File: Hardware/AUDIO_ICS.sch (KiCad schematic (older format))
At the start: 41 parts, among them U10 PCM1863, U9 PCM9211, X1 24.576 MHz

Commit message: Completed placement of level shifters
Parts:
- C36: footprint Capacitors_SMD:c_elec_4x4.5 -> Capacitors_SMD:C_1206
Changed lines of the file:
@@
 F 0 "C36" H 1750 10700 40  0000 L CNN
 F 1 "10uF" H 1756 10515 40  0000 L CNN
-F 2 "Capacitors_SMD:c_elec_4x4.5" H 1788 10450 30  0001 C CNN
+F 2 "Capacitors_SMD:C_1206" H 1788 10450 30  0001 C CNN
 F 3 "" H 1750 10600 60  0000 C CNN
 	1    1750 10600
@@
 	6000 4950 6000 4400
 Wire Wire Line
-	5450 4950 5700 4950
-Wire Wire Line
-	5700 4950 6000 4950
+	5450 4950 6000 4950
 Wire Wire Line
 	2850 4500 2850 5100
@@
 	4800 2000 6000 2000
 Wire Wire Line
-	6100 7450 6100 7550
-Wire Wire Line
-	6100 7550 6100 9700
+	6100 7450 6100 9700
 Wire Wire Line
 	6300 2200 4800 2200
@@
 Connection ~ 5400 1500
 Wire Wire Line
-	5100 1500 5400 1500
-Wire Wire Line
-	5400 1500 5550 1500
-Wire Wire Line
-	5550 1500 5700 1500
-Wire Wire Line
-	5700 1500 6000 1500
+	5100 1500 6000 1500
 Wire Wire Line
 	5100 1500 5100 1350
@@
 	2800 10900 2800 11000
 Wire Wire Line
-	2650 10900 2800 10900
-Wire Wire Line
-	2800 10900 2950 10900
+	2650 10900 2950 10900
 Wire Wire Line
 	2650 10750 2650 10900
@@
 	2800 10300 2800 10250
 Wire Wire Line
-	2650 10300 2800 10300
-Wire Wire Line
-	2800 10300 2950 10300
+	2650 10300 2950 10300
 Wire Wire Line
 	2650 10300 2650 10450
@@
 	1750 10750 1750 10900
 Wire Wire Line
-	1750 10900 1750 10900
-Wire Wire Line
-	1750 10900 1900 10900
-Wire Wire Line
-	1900 10900 2050 10900
-Wire Wire Line
-	2050 10900 2050 10900
+	1750 10900 2050 10900
 Wire Wire Line
 	1900 10900 1900 11000
@@
 	1900 10300 1900 10250
 Wire Wire Line
-	1750 10300 1750 10300
-Wire Wire Line
-	1750 10300 1900 10300
-Wire Wire Line
-	1900 10300 2050 10300
-Wire Wire Line
-	2050 10300 2050 10300
+	1750 10300 2050 10300
 Wire Wire Line
 	1750 10300 1750 10450
@@
 Connection ~ 2950 2600
 Wire Wire Line
-	2950 2500 2950 2600
-Wire Wire Line
-	2950 2600 2950 2900
+	2950 2500 2950 2900
 Wire Wire Line
 	2950 2600 3100 2600
@@
 	2950 1500 3100 1500
 Wire Wire Line
-	2950 1300 2950 1500
-Wire Wire Line
-	2950 1500 2950 1600
-Wire Wire Line
-	2950 1600 2950 1700
+	2950 1300 2950 1700
 Wire Wire Line
 	2950 2000 3100 2000
 Wire Wire Line
-	2950 1800 2950 2000
-Wire Wire Line
-	2950 2000 2950 2250
+	2950 1800 2950 2250
 Wire Wire Line
 	3100 2100 2300 2100
@@
 	2100 4850 2250 4850
 Wire Wire Line
-	2100 4100 2100 4500
-Wire Wire Line
-	2100 4500 2100 4850
-Wire Wire Line
-	2100 4850 2100 5100
+	2100 4100 2100 5100
 Wire Wire Line
 	2100 4100 2250 4100
@@
 	5700 3800 5700 4550
 Wire Wire Line
-	4800 3800 5450 3800
-Wire Wire Line
-	5450 3800 5700 3800
+	4800 3800 5700 3800
 Wire Wire Line
 	5450 3800 5450 4000
@@
 	5300 4200 4800 4200
 Wire Wire Line
-	5300 4000 5300 4100
-Wire Wire Line
-	5300 4100 5300 4200
-Wire Wire Line
-	5300 4200 5300 4300
-Wire Wire Line
-	5300 4300 5300 5100
+	5300 4000 5300 5100
 Wire Wire Line
 	5300 4300 4800 4300
@@
 	4900 4400 4900 4550
 Wire Wire Line
-	4800 4400 4900 4400
-Wire Wire Line
-	4900 4400 5150 4400
-Wire Wire Line
-	1650 7000 1950 7000
-Wire Wire Line
-	1950 7000 3350 7000
-Wire Wire Line
-	1650 6800 2100 6800
-Wire Wire Line
-	2100 6800 3350 6800
-Wire Wire Line
-	1650 6550 2250 6550
-Wire Wire Line
-	2250 6550 3350 6550
-Wire Wire Line
-	1650 6350 2400 6350
-Wire Wire Line
-	2400 6350 3350 6350
+	4800 4400 5150 4400
+Wire Wire Line
+	1650 7000 3350 7000
+Wire Wire Line
+	1650 6800 3350 6800
+Wire Wire Line
+	1650 6550 3350 6550
+Wire Wire Line
+	1650 6350 3350 6350
 Wire Wire Line
 	2400 7450 2400 7600
@@
 Connection ~ 2700 4100
 Wire Wire Line
-	2550 4100 2700 4100
-Wire Wire Line
-	2700 4100 3100 4100
+	2550 4100 3100 4100
 Wire Wire Line
 	2700 4100 2700 4300
 Wire Wire Line
-	2550 4850 2700 4850
-Wire Wire Line
-	2700 4850 2950 4850
+	2550 4850 2950 4850
 Wire Wire Line
 	2700 4700 2700 4850
 Wire Wire Line
-	4150 6150 4150 6800
-Wire Wire Line
-	4150 6800 4150 6900
+	4150 6150 4150 6900
 Wire Wire Line
 	4150 6800 4250 6800
@@
 	4250 8750 4250 9050
 Wire Wire Line
-	5950 8550 5950 8650
-Wire Wire Line
-	5950 8650 5950 8750
-Wire Wire Line
-	5950 8750 5950 9700
+	5950 8550 5950 9700
 Wire Wire Line
 	5950 8750 5850 8750
@@
 	3900 7200 4250 7200
 Wire Wire Line
-	1650 7850 2400 7850
-Wire Wire Line
-	2400 7850 3200 7850
-Wire Wire Line
-	3200 7850 3350 7850
-Wire Wire Line
-	1650 8050 2250 8050
-Wire Wire Line
-	2250 8050 3050 8050
-Wire Wire Line
-	3050 8050 3350 8050
-Wire Wire Line
-	1650 8300 2100 8300
-Wire Wire Line
-	2100 8300 2900 8300
-Wire Wire Line
-	2900 8300 3350 8300
-Wire Wire Line
-	1650 8500 1950 8500
-Wire Wire Line
-	1950 8500 2750 8500
-Wire Wire Line
-	2750 8500 3350 8500
+	1650 7850 3350 7850
+Wire Wire Line
+	1650 8050 3350 8050
+Wire Wire Line
+	1650 8300 3350 8300
+Wire Wire Line
+	1650 8500 3350 8500
 Wire Wire Line
 	2400 9350 2400 9700
@@
 	3950 9350 3950 9700
 Wire Wire Line
-	3950 8200 3950 8900
-Wire Wire Line
-	3950 8900 3950 9050
+	3950 8200 3950 9050
 Wire Wire Line
 	3950 8200 4250 8200
@@
 	3200 9550 3200 9350
 Wire Wire Line
-	2750 9550 2900 9550
-Wire Wire Line
-	2900 9550 3050 9550
-Wire Wire Line
-	3050 9550 3200 9550
-Wire Wire Line
-	3200 9550 3550 9550
+	2750 9550 3550 9550
 Wire Wire Line
 	3550 9550 3550 8900
@@
 Connection ~ 5700 1500
 Wire Wire Line
-	5100 900  5400 900
-Wire Wire Line
-	5400 900  5550 900
-Wire Wire Line
-	5550 900  5700 900
-Wire Wire Line
-	5700 900  6000 900
+	5100 900  6000 900
 Connection ~ 5550 900
 Wire Wire Line

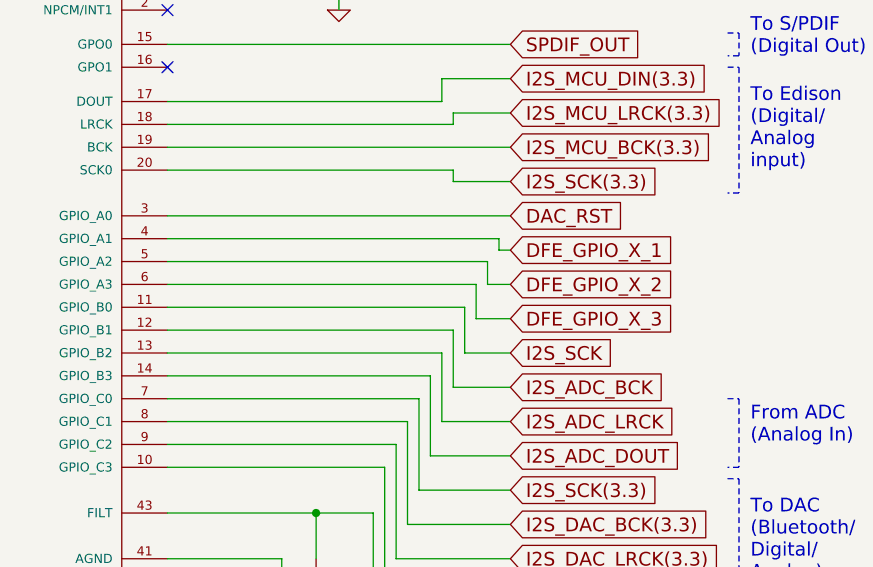
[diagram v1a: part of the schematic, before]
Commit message: Digital Half completed placement
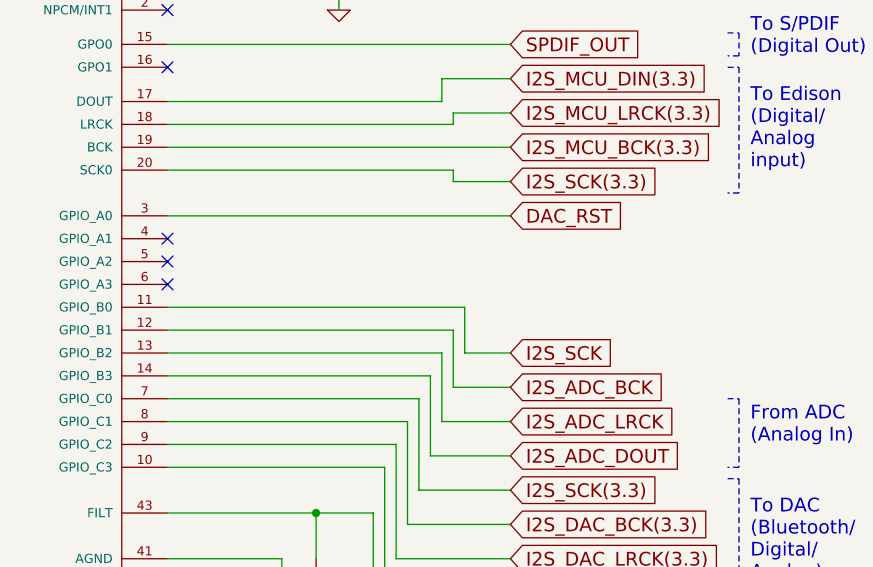
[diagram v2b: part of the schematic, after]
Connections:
- net DFE_GPIO_X_1: no longer names the net of U9.4 (GPIO_A1)
- net DFE_GPIO_X_2: no longer names the net of U9.5 (GPIO_A2)
- net DFE_GPIO_X_3: no longer names the net of U9.6 (GPIO_A3)
- no-connect marks 12 -> 15
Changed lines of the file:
@@
 ADC unused\nAnalog VCC\nGrounded
 $Comp
-L +3.3VSB #PWR039
+L +3.3VSB #PWR036
 U 1 1 57F2FC3A
 P 2950 1300
-F 0 "#PWR039" H 2950 1260 30  0001 C CNN
+F 0 "#PWR036" H 2950 1260 30  0001 C CNN
 F 1 "+3.3VSB" H 2950 1400 30  0000 C CNN
 F 2 "" H 2950 1300 60  0000 C CNN
@@
 Pulled LOW for\nI2C mode
 $Comp
-L GND-RESCUE-museV2-RESCUE-museV2 #PWR040
+L GND-RESCUE-museV2-RESCUE-museV2 #PWR037
 U 1 1 57F2FC41
 P 2950 2250
-F 0 "#PWR040" H 2950 2250 30  0001 C CNN
+F 0 "#PWR037" H 2950 2250 30  0001 C CNN
 F 1 "GND" H 2950 2180 30  0001 C CNN
 F 2 "" H 2950 2250 60  0000 C CNN
@@
 $EndComp
 $Comp
-L GND-RESCUE-museV2-RESCUE-museV2 #PWR041
+L GND-RESCUE-museV2-RESCUE-museV2 #PWR038
 U 1 1 57F2FC5D
 P 2100 5100
-F 0 "#PWR041" H 2100 5100 30  0001 C CNN
+F 0 "#PWR038" H 2100 5100 30  0001 C CNN
 F 1 "GND" H 2100 5030 30  0001 C CNN
 F 2 "" H 2100 5100 60  0000 C CNN
@@
 $EndComp
 $Comp
-L GND-RESCUE-museV2-RESCUE-museV2 #PWR042
+L GND-RESCUE-museV2-RESCUE-museV2 #PWR039
 U 1 1 57F2FC84
 P 5300 5100
-F 0 "#PWR042" H 5300 5100 30  0001 C CNN
+F 0 "#PWR039" H 5300 5100 30  0001 C CNN
 F 1 "GND" H 5300 5030 30  0001 C CNN
 F 2 "" H 5300 5100 60  0000 C CNN
@@
 $EndComp
 $Comp
-L GND-RESCUE-museV2-RESCUE-museV2 #PWR043
+L GND-RESCUE-museV2-RESCUE-museV2 #PWR040
 U 1 1 57F2FC8A
 P 5150 5100
-F 0 "#PWR043" H 5150 5100 30  0001 C CNN
+F 0 "#PWR040" H 5150 5100 30  0001 C CNN
 F 1 "GND" H 5150 5030 30  0001 C CNN
 F 2 "" H 5150 5100 60  0000 C CNN
@@
 $EndComp
 $Comp
-L GND-RESCUE-museV2-RESCUE-museV2 #PWR044
+L GND-RESCUE-museV2-RESCUE-museV2 #PWR041
 U 1 1 57F2FC90
 P 4900 5100
-F 0 "#PWR044" H 4900 5100 30  0001 C CNN
+F 0 "#PWR041" H 4900 5100 30  0001 C CNN
 F 1 "GND" H 4900 5030 30  0001 C CNN
 F 2 "" H 4900 5100 60  0000 C CNN
@@
 $EndComp
 $Comp
-L GND-RESCUE-museV2-RESCUE-museV2 #PWR045
+L GND-RESCUE-museV2-RESCUE-museV2 #PWR042
 U 1 1 57F2FCAF
 P 2400 7600
-F 0 "#PWR045" H 2400 7600 30  0001 C CNN
+F 0 "#PWR042" H 2400 7600 30  0001 C CNN
 F 1 "GND" H 2400 7530 30  0001 C CNN
 F 2 "" H 2400 7600 60  0000 C CNN
@@
 $EndComp
 $Comp
-L GND-RESCUE-museV2-RESCUE-museV2 #PWR046
+L GND-RESCUE-museV2-RESCUE-museV2 #PWR043
 U 1 1 57F2FCB5
 P 2250 7600
-F 0 "#PWR046" H 2250 7600 30  0001 C CNN
+F 0 "#PWR043" H 2250 7600 30  0001 C CNN
 F 1 "GND" H 2250 7530 30  0001 C CNN
 F 2 "" H 2250 7600 60  0000 C CNN
@@
 $EndComp
 $Comp
-L GND-RESCUE-museV2-RESCUE-museV2 #PWR047
+L GND-RESCUE-museV2-RESCUE-museV2 #PWR044
 U 1 1 57F2FCBB
 P 2100 7600
-F 0 "#PWR047" H 2100 7600 30  0001 C CNN
+F 0 "#PWR044" H 2100 7600 30  0001 C CNN
 F 1 "GND" H 2100 7530 30  0001 C CNN
 F 2 "" H 2100 7600 60  0000 C CNN
@@
 $EndComp
 $Comp
-L GND-RESCUE-museV2-RESCUE-museV2 #PWR048
+L GND-RESCUE-museV2-RESCUE-museV2 #PWR045
 U 1 1 57F2FCC1
 P 1950 7600
-F 0 "#PWR048" H 1950 7600 30  0001 C CNN
+F 0 "#PWR045" H 1950 7600 30  0001 C CNN
 F 1 "GND" H 1950 7530 30  0001 C CNN
 F 2 "" H 1950 7600 60  0000 C CNN
@@
 $EndComp
 $Comp
-L +3.3VSB #PWR049
+L +3.3VSB #PWR046
 U 1 1 57F2FD06
 P 4150 6150
-F 0 "#PWR049" H 4150 6110 30  0001 C CNN
+F 0 "#PWR046" H 4150 6110 30  0001 C CNN
 F 1 "+3.3VSB" H 4150 6260 30  0000 C CNN
 F 2 "" H 4150 6150 60  0000 C CNN
@@
 $EndComp
 $Comp
-L +1.8VSB #PWR050
+L +1.8VSB #PWR047
 U 1 1 57F2FD0C
 P 3950 6150
-F 0 "#PWR050" H 3950 6290 20  0001 C CNN
+F 0 "#PWR047" H 3950 6290 20  0001 C CNN
 F 1 "+1.8VSB" H 3950 6260 30  0000 C CNN
 F 2 "" H 3950 6150 60  0000 C CNN
@@
 PCM1863 (ADC)
 $Comp
-L GND-RESCUE-museV2-RESCUE-museV2 #PWR051
+L GND-RESCUE-museV2-RESCUE-museV2 #PWR048
 U 1 1 57F2FD1E
 P 5950 9700
-F 0 "#PWR051" H 5950 9700 30  0001 C CNN
+F 0 "#PWR048" H 5950 9700 30  0001 C CNN
 F 1 "GND" H 5950 9630 30  0001 C CNN
 F 2 "" H 5950 9700 60  0000 C CNN
@@
 $EndComp
 $Comp
-L GND-RESCUE-museV2-RESCUE-museV2 #PWR052
+L GND-RESCUE-museV2-RESCUE-museV2 #PWR049
 U 1 1 57F2FD2B
 P 4250 9700
-F 0 "#PWR052" H 4250 9700 30  0001 C CNN
+F 0 "#PWR049" H 4250 9700 30  0001 C CNN
 F 1 "GND" H 4250 9630 30  0001 C CNN
 F 2 "" H 4250 9700 60  0000 C CNN
@@
 $EndComp
 $Comp
-L GND-RESCUE-museV2-RESCUE-museV2 #PWR053
+L GND-RESCUE-museV2-RESCUE-museV2 #PWR050
 U 1 1 57F2FD4E
 P 2400 9700
-F 0 "#PWR053" H 2400 9700 30  0001 C CNN
+F 0 "#PWR050" H 2400 9700 30  0001 C CNN
 F 1 "GND" H 2400 9630 30  0001 C CNN
 F 2 "" H 2400 9700 60  0000 C CNN
@@
 $EndComp
 $Comp
-L GND-RESCUE-museV2-RESCUE-museV2 #PWR054
+L GND-RESCUE-museV2-RESCUE-museV2 #PWR051
 U 1 1 57F2FD54
 P 2250 9700
-F 0 "#PWR054" H 2250 9700 30  0001 C CNN
+F 0 "#PWR051" H 2250 9700 30  0001 C CNN
 F 1 "GND" H 2250 9630 30  0001 C CNN
 F 2 "" H 2250 9700 60  0000 C CNN
@@
 $EndComp
 $Comp
-L GND-RESCUE-museV2-RESCUE-museV2 #PWR055
+L GND-RESCUE-museV2-RESCUE-museV2 #PWR052
 U 1 1 57F2FD5A
 P 2100 9700
-F 0 "#PWR055" H 2100 9700 30  0001 C CNN
+F 0 "#PWR052" H 2100 9700 30  0001 C CNN
 F 1 "GND" H 2100 9630 30  0001 C CNN
 F 2 "" H 2100 9700 60  0000 C CNN
@@
 $EndComp
 $Comp
-L GND-RESCUE-museV2-RESCUE-museV2 #PWR056
+L GND-RESCUE-museV2-RESCUE-museV2 #PWR053
 U 1 1 57F2FD60
 P 1950 9700
-F 0 "#PWR056" H 1950 9700 30  0001 C CNN
+F 0 "#PWR053" H 1950 9700 30  0001 C CNN
 F 1 "GND" H 1950 9630 30  0001 C CNN
 F 2 "" H 1950 9700 60  0000 C CNN
@@
 $EndComp
 $Comp
-L GND-RESCUE-museV2-RESCUE-museV2 #PWR057
+L GND-RESCUE-museV2-RESCUE-museV2 #PWR054
 U 1 1 57F2FD94
 P 3950 9700
-F 0 "#PWR057" H 3950 9700 30  0001 C CNN
+F 0 "#PWR054" H 3950 9700 30  0001 C CNN
 F 1 "GND" H 3950 9630 30  0001 C CNN
 F 2 "" H 3950 9700 60  0000 C CNN
@@
 From Edison\n(Bluetooth/\nAnalog input)
 $Comp
-L +3.3VSB #PWR058
+L +3.3VSB #PWR055
 U 1 1 57F2FDC3
 P 2950 2500
-F 0 "#PWR058" H 2950 2460 30  0001 C CNN
+F 0 "#PWR055" H 2950 2460 30  0001 C CNN
 F 1 "+3.3VSB" H 2950 2600 30  0000 C CNN
 F 2 "" H 2950 2500 60  0000 C CNN
@@
 $EndComp
 $Comp
-L GND-RESCUE-museV2-RESCUE-museV2 #PWR059
+L GND-RESCUE-museV2-RESCUE-museV2 #PWR056
 U 1 1 57F2FDC9
 P 6100 9700
-F 0 "#PWR059" H 6100 9700 30  0001 C CNN
+F 0 "#PWR056" H 6100 9700 30  0001 C CNN
 F 1 "GND" H 6100 9630 30  0001 C CNN
 F 2 "" H 6100 9700 60  0000 C CNN
@@
 Decoupling Capacitors
 $Comp
-L +1.8VSB #PWR060
+L +1.8VSB #PWR057
 U 1 1 57FA08B9
 P 2800 10250
-F 0 "#PWR060" H 2800 10390 20  0001 C CNN
+F 0 "#PWR057" H 2800 10390 20  0001 C CNN
 F 1 "+1.8VSB" H 2800 10360 30  0000 C CNN
 F 2 "" H 2800 10250 60  0000 C CNN
@@
 $EndComp
 $Comp
-L GND-RESCUE-museV2-RESCUE-museV2 #PWR061
+L GND-RESCUE-museV2-RESCUE-museV2 #PWR058
 U 1 1 57FA08BF
 P 2800 11000
-F 0 "#PWR061" H 2800 11000 30  0001 C CNN
+F 0 "#PWR058" H 2800 11000 30  0001 C CNN
 F 1 "GND" H 2800 10930 30  0001 C CNN
 F 2 "" H 2800 11000 60  0000 C CNN
@@
 $EndComp
 $Comp
-L GND-RESCUE-museV2-RESCUE-museV2 #PWR062
+L GND-RESCUE-museV2-RESCUE-museV2 #PWR059
 U 1 1 57FA08D3
 P 1900 11000
-F 0 "#PWR062" H 1900 11000 30  0001 C CNN
+F 0 "#PWR059" H 1900 11000 30  0001 C CNN
 F 1 "GND" H 1900 10930 30  0001 C CNN
 F 2 "" H 1900 11000 60  0000 C CNN
@@
 $EndComp
 $Comp
-L +3.3VSB #PWR063
+L +3.3VSB #PWR060
 U 1 1 57FA08F5
 P 1900 10250
-F 0 "#PWR063" H 1900 10210 30  0001 C CNN
+F 0 "#PWR060" H 1900 10210 30  0001 C CNN
 F 1 "+3.3VSB" H 1900 10360 30  0000 C CNN
 F 2 "" H 1900 10250 60  0000 C CNN
@@
 $EndComp
 $Comp
-L GND-RESCUE-museV2-RESCUE-museV2 #PWR064
+L GND-RESCUE-museV2-RESCUE-museV2 #PWR061
 U 1 1 57FA1F81
 P 5550 1600
-F 0 "#PWR064" H 5550 1600 30  0001 C CNN
+F 0 "#PWR061" H 5550 1600 30  0001 C CNN
 F 1 "GND" H 5550 1530 30  0001 C CNN
 F 2 "" H 5550 1600 60  0000 C CNN
@@
 $EndComp
 $Comp
-L +3.3VSB #PWR065
+L +3.3VSB #PWR062
 U 1 1 57FA1FAB
 P 5550 800
-F 0 "#PWR065" H 5550 760 30  0001 C CNN
+F 0 "#PWR062" H 5550 760 30  0001 C CNN
 F 1 "+3.3VSB" H 5550 910 30  0000 C CNN
 F 2 "" H 5550 800 60  0000 C CNN
@@
 Text GLabel 6300 3250 2    60   Input ~ 0
 I2S_ADC_BCK
-Text GLabel 6300 2950 2    60   Input ~ 0
-DFE_GPIO_X_3
-Text GLabel 6300 2800 2    60   Input ~ 0
-DFE_GPIO_X_2
-Text GLabel 6300 2650 2    60   Input ~ 0
-DFE_GPIO_X_1
 Text GLabel 6400 7650 2    60   Input ~ 0
 I2S_ADC_LRCK
@@
 Minimize oscilator traces as \nmuch as possible
 $Comp
-L GND-RESCUE-museV2-RESCUE-museV2 #PWR066
+L GND-RESCUE-museV2-RESCUE-museV2 #PWR063
 U 1 1 58601EEE
 P 2850 5100
-F 0 "#PWR066" H 2850 5100 30  0001 C CNN
+F 0 "#PWR063" H 2850 5100 30  0001 C CNN
 F 1 "GND" H 2850 5030 30  0001 C CNN
 F 2 "" H 2850 5100 60  0000 C CNN
@@
 $EndComp
 $Comp
-L +3.3VSB #PWR067
+L +3.3VSB #PWR064
 U 1 1 5860C610
 P 6000 4400
-F 0 "#PWR067" H 6000 4360 30  0001 C CNN
+F 0 "#PWR064" H 6000 4360 30  0001 C CNN
 F 1 "+3.3VSB" H 6000 4500 30  0000 C CNN
 F 2 "" H 6000 4400 60  0000 C CNN
@@
 Wire Wire Line
 	6300 7700 6300 7650
-Wire Wire Line
-	6250 2650 6300 2650
-Wire Wire Line
-	6250 2600 6250 2650
-Wire Wire Line
-	4800 2600 6250 2600
-Wire Wire Line
-	6200 2700 4800 2700
-Wire Wire Line
-	6200 2800 6200 2700
-Wire Wire Line
-	6300 2800 6200 2800
-Wire Wire Line
-	6150 2800 4800 2800
-Wire Wire Line
-	6150 2950 6150 2800
-Wire Wire Line
-	6300 2950 6150 2950
 Wire Wire Line
 	6050 2350 6300 2350
@@
 	5550 1600 5550 1500
 Connection ~ 5550 1500
+NoConn ~ 4800 2800
+NoConn ~ 4800 2700
+NoConn ~ 4800 2600
 $EndSCHEMATC

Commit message: Beginning analog chip placement
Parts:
- C15, C17, C22, C36: footprint Capacitors_SMD:C_1206 -> Capacitors_SMD:c_elec_4x5.3
- C24, C26, C27, C28, C29, C30, C31, C32, C33: footprint Capacitors_SMD:c_elec_4x4.5 -> Capacitors_SMD:c_elec_4x5.3
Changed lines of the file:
@@
 F 0 "C24" H 5700 4800 40  0000 L CNN
 F 1 "4700pF" H 5706 4615 40  0000 L CNN
-F 2 "Capacitors_SMD:c_elec_4x4.5" H 5738 4550 30  0001 C CNN
+F 2 "Capacitors_SMD:c_elec_4x5.3" H 5738 4550 30  0001 C CNN
 F 3 "" H 5700 4700 60  0000 C CNN
 	1    5700 4700
@@
 F 0 "C22" H 5150 4800 40  0000 L CNN
 F 1 "10uF" H 5156 4615 40  0000 L CNN
-F 2 "Capacitors_SMD:C_1206" H 5188 4550 30  0001 C CNN
+F 2 "Capacitors_SMD:c_elec_4x5.3" H 5188 4550 30  0001 C CNN
 F 3 "" H 5150 4700 60  0000 C CNN
 	1    5150 4700
@@
 F 0 "C26" V 3550 6450 40  0000 L CNN
 F 1 "10uF" V 3550 6150 40  0000 L CNN
-F 2 "Capacitors_SMD:c_elec_4x4.5" H 3538 6200 30  0001 C CNN
+F 2 "Capacitors_SMD:c_elec_4x5.3" H 3538 6200 30  0001 C CNN
 F 3 "" H 3500 6350 60  0000 C CNN
 	1    3500 6350
@@
 F 0 "C27" V 3550 6650 40  0000 L CNN
 F 1 "10uF" V 3550 6350 40  0000 L CNN
-F 2 "Capacitors_SMD:c_elec_4x4.5" H 3538 6400 30  0001 C CNN
+F 2 "Capacitors_SMD:c_elec_4x5.3" H 3538 6400 30  0001 C CNN
 F 3 "" H 3500 6550 60  0000 C CNN
 	1    3500 6550
@@
 F 0 "C29" V 3550 7100 40  0000 L CNN
 F 1 "10uF" V 3550 6800 40  0000 L CNN
-F 2 "Capacitors_SMD:c_elec_4x4.5" H 3538 6850 30  0001 C CNN
+F 2 "Capacitors_SMD:c_elec_4x5.3" H 3538 6850 30  0001 C CNN
 F 3 "" H 3500 7000 60  0000 C CNN
 	1    3500 7000
@@
 F 0 "C28" V 3550 6900 40  0000 L CNN
 F 1 "10uF" V 3550 6600 40  0000 L CNN
-F 2 "Capacitors_SMD:c_elec_4x4.5" H 3538 6650 30  0001 C CNN
+F 2 "Capacitors_SMD:c_elec_4x5.3" H 3538 6650 30  0001 C CNN
 F 3 "" H 3500 6800 60  0000 C CNN
 	1    3500 6800
@@
 F 0 "C30" V 3550 7950 40  0000 L CNN
 F 1 "10uF" V 3550 7650 40  0000 L CNN
-F 2 "Capacitors_SMD:c_elec_4x4.5" H 3538 7700 30  0001 C CNN
+F 2 "Capacitors_SMD:c_elec_4x5.3" H 3538 7700 30  0001 C CNN
 F 3 "" H 3500 7850 60  0000 C CNN
 	1    3500 7850
@@
 F 0 "C31" V 3550 8150 40  0000 L CNN
 F 1 "10uF" V 3550 7850 40  0000 L CNN
-F 2 "Capacitors_SMD:c_elec_4x4.5" H 3538 7900 30  0001 C CNN
+F 2 "Capacitors_SMD:c_elec_4x5.3" H 3538 7900 30  0001 C CNN
 F 3 "" H 3500 8050 60  0000 C CNN
 	1    3500 8050
@@
 F 0 "C33" V 3550 8600 40  0000 L CNN
 F 1 "10uF" V 3550 8300 40  0000 L CNN
-F 2 "Capacitors_SMD:c_elec_4x4.5" H 3538 8350 30  0001 C CNN
+F 2 "Capacitors_SMD:c_elec_4x5.3" H 3538 8350 30  0001 C CNN
 F 3 "" H 3500 8500 60  0000 C CNN
 	1    3500 8500
@@
 F 0 "C32" V 3550 8400 40  0000 L CNN
 F 1 "10uF" V 3550 8100 40  0000 L CNN
-F 2 "Capacitors_SMD:c_elec_4x4.5" H 3538 8150 30  0001 C CNN
+F 2 "Capacitors_SMD:c_elec_4x5.3" H 3538 8150 30  0001 C CNN
 F 3 "" H 3500 8300 60  0000 C CNN
 	1    3500 8300
@@
 F 0 "C36" H 1750 10700 40  0000 L CNN
 F 1 "10uF" H 1756 10515 40  0000 L CNN
-F 2 "Capacitors_SMD:C_1206" H 1788 10450 30  0001 C CNN
+F 2 "Capacitors_SMD:c_elec_4x5.3" H 1788 10450 30  0001 C CNN
 F 3 "" H 1750 10600 60  0000 C CNN
 	1    1750 10600
@@
 F 0 "C15" H 5100 1300 40  0000 L CNN
 F 1 "10uF" H 5106 1115 40  0000 L CNN
-F 2 "Capacitors_SMD:C_1206" H 5138 1050 30  0001 C CNN
+F 2 "Capacitors_SMD:c_elec_4x5.3" H 5138 1050 30  0001 C CNN
 F 3 "" H 5100 1200 60  0000 C CNN
 	1    5100 1200
@@
 F 0 "C17" H 5700 1300 40  0000 L CNN
 F 1 "10uF" H 5706 1115 40  0000 L CNN
-F 2 "Capacitors_SMD:C_1206" H 5738 1050 30  0001 C CNN
+F 2 "Capacitors_SMD:c_elec_4x5.3" H 5738 1050 30  0001 C CNN
 F 3 "" H 5700 1200 60  0000 C CNN
 	1    5700 1200
